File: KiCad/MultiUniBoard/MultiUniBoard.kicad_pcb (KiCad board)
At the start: 2 copper layers, 75.6 x 63.5 mm, 5 parts

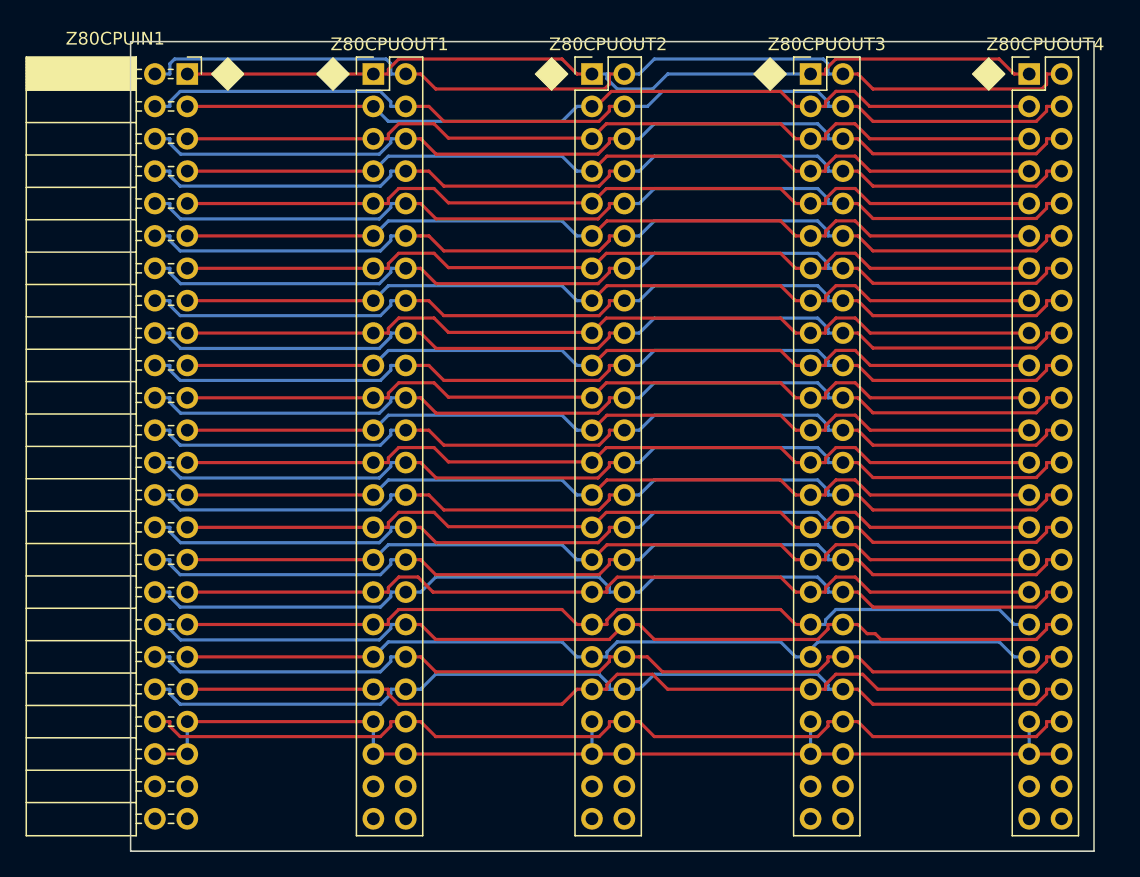
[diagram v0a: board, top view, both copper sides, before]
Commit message: Fix several problems with Chip Select. Reconnect the Data bus for the VDG to the CPU bus which has become disconnected.
Signed-off-by: John Bradley <flypie@rocketmail.com>
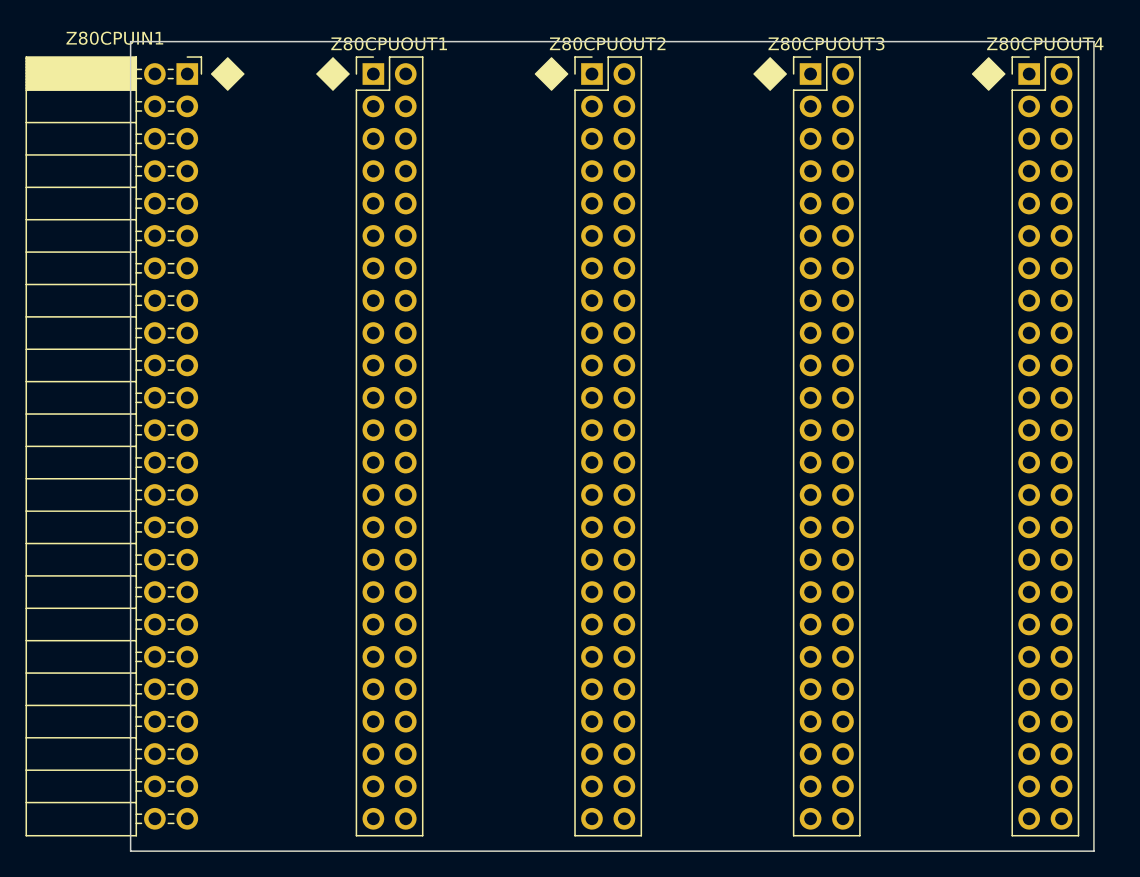
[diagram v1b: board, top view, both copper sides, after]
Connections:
- Z80CPUIN1 pad 45: Net-(Z80CPUIN1-Pad45) -> (no net)
- Z80CPUIN1 pad 46: Net-(Z80CPUIN1-Pad46) -> (no net)
- Z80CPUIN1 pad 47: Net-(Z80CPUIN1-Pad47) -> (no net)
- Z80CPUIN1 pad 48: Net-(Z80CPUIN1-Pad48) -> (no net)
- Z80CPUOUT1 pad 45: Net-(Z80CPUOUT1-Pad45) -> (no net)
- Z80CPUOUT1 pad 46: Net-(Z80CPUOUT1-Pad46) -> (no net)
- Z80CPUOUT1 pad 47: Net-(Z80CPUOUT1-Pad47) -> (no net)
- Z80CPUOUT1 pad 48: Net-(Z80CPUOUT1-Pad48) -> (no net)
- Z80CPUOUT2 pad 45: Net-(Z80CPUOUT2-Pad45) -> (no net)
- Z80CPUOUT2 pad 46: Net-(Z80CPUOUT2-Pad46) -> (no net)
- Z80CPUOUT2 pad 47: Net-(Z80CPUOUT2-Pad47) -> (no net)
- Z80CPUOUT2 pad 48: Net-(Z80CPUOUT2-Pad48) -> (no net)
- Z80CPUOUT3 pad 45: Net-(Z80CPUOUT3-Pad45) -> (no net)
- Z80CPUOUT3 pad 46: Net-(Z80CPUOUT3-Pad46) -> (no net)
- Z80CPUOUT3 pad 47: Net-(Z80CPUOUT3-Pad47) -> (no net)
- Z80CPUOUT3 pad 48: Net-(Z80CPUOUT3-Pad48) -> (no net)
- Z80CPUOUT4 pad 45: Net-(Z80CPUOUT4-Pad45) -> (no net)
- Z80CPUOUT4 pad 46: Net-(Z80CPUOUT4-Pad46) -> (no net)
- Z80CPUOUT4 pad 47: Net-(Z80CPUOUT4-Pad47) -> (no net)
- Z80CPUOUT4 pad 48: Net-(Z80CPUOUT4-Pad48) -> (no net)
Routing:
- net GND: track 83.8 -> 0.00 mm
- net /DA7: track 77.4 -> 0.00 mm
- net /A6: track 76.1 -> 0.00 mm
- net /A4: track 76.1 -> 0.00 mm
- net /A1: track 76.1 -> 0.00 mm
- net /~NMI: track 76.1 -> 0.00 mm
- net /~IOREQ: track 76.1 -> 0.00 mm
- net /DA2: track 76.1 -> 0.00 mm
- net /~INT: track 76.1 -> 0.00 mm
- net /~BUSAK: track 76.1 -> 0.00 mm
- net /~RD: track 76.1 -> 0.00 mm
- net /~M1: track 76.1 -> 0.00 mm
- net /~BUSRQ: track 76.1 -> 0.00 mm
- net /~HALT: track 76.1 -> 0.00 mm
- net /~WR: track 76.1 -> 0.00 mm
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
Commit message: First complete system. Unlikely to work but will serve as the basis of a system to test VGA.
Signed-off-by: John Bradley <flypie@rocketmail.com>
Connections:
- net /~BUSAK renamed /~{BUSAK}
- net /~BUSRQ renamed /~{BUSRQ}
- net /~CPUCLK renamed /~{CPUCLK}
- net /~HALT renamed /~{HALT}
- net /~INT renamed /~{INT}
- net /~IOREQ renamed /~{IOREQ}
- net /~M1 renamed /~{M1}
- net /~MREQ renamed /~{MREQ}
- net /~NMI renamed /~{NMI}
- net /~RD renamed /~{RD}
- net /~REFSH renamed /~{REFSH}
- net /~RESET renamed /~{RESET}
- net /~WAIT renamed /~{WAIT}
- net /~WE renamed /~{WE}
- net /~WR renamed /~{WR}
- Z80CPUIN1 pad 45: (no net) -> unconnected-(Z80CPUIN1-Pad45)
- Z80CPUIN1 pad 46: (no net) -> unconnected-(Z80CPUIN1-Pad46)
- Z80CPUIN1 pad 47: (no net) -> unconnected-(Z80CPUIN1-Pad47)
- Z80CPUIN1 pad 48: (no net) -> unconnected-(Z80CPUIN1-Pad48)
- Z80CPUOUT1 pad 45: (no net) -> unconnected-(Z80CPUOUT1-Pad45)
- Z80CPUOUT1 pad 46: (no net) -> unconnected-(Z80CPUOUT1-Pad46)
- Z80CPUOUT1 pad 47: (no net) -> unconnected-(Z80CPUOUT1-Pad47)
- Z80CPUOUT1 pad 48: (no net) -> unconnected-(Z80CPUOUT1-Pad48)
- Z80CPUOUT2 pad 45: (no net) -> unconnected-(Z80CPUOUT2-Pad45)
- Z80CPUOUT2 pad 46: (no net) -> unconnected-(Z80CPUOUT2-Pad46)
- Z80CPUOUT2 pad 47: (no net) -> unconnected-(Z80CPUOUT2-Pad47)
- Z80CPUOUT2 pad 48: (no net) -> unconnected-(Z80CPUOUT2-Pad48)
- Z80CPUOUT3 pad 45: (no net) -> unconnected-(Z80CPUOUT3-Pad45)
- Z80CPUOUT3 pad 46: (no net) -> unconnected-(Z80CPUOUT3-Pad46)
- Z80CPUOUT3 pad 47: (no net) -> unconnected-(Z80CPUOUT3-Pad47)
- Z80CPUOUT3 pad 48: (no net) -> unconnected-(Z80CPUOUT3-Pad48)
- Z80CPUOUT4 pad 45: (no net) -> unconnected-(Z80CPUOUT4-Pad45)
- Z80CPUOUT4 pad 46: (no net) -> unconnected-(Z80CPUOUT4-Pad46)
- Z80CPUOUT4 pad 47: (no net) -> unconnected-(Z80CPUOUT4-Pad47)
- Z80CPUOUT4 pad 48: (no net) -> unconnected-(Z80CPUOUT4-Pad48)
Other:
- net class Default removed
